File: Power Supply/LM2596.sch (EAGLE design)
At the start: 11 parts

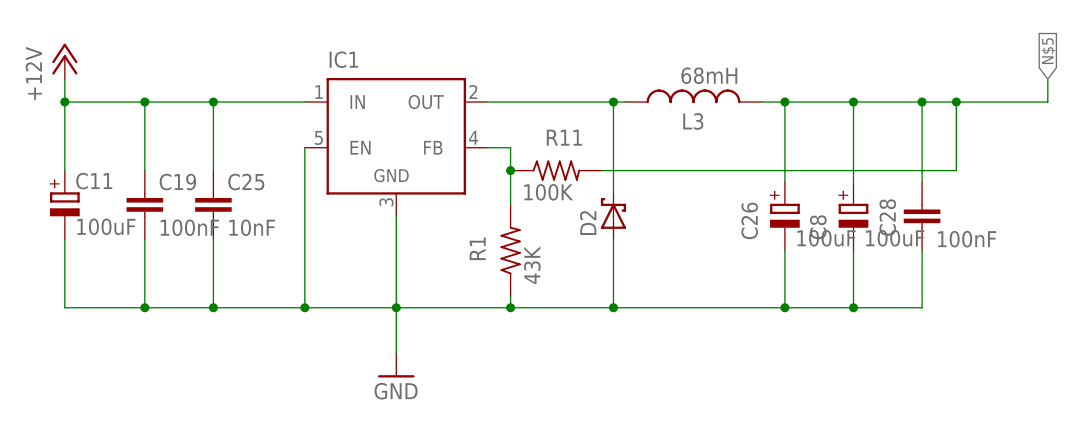
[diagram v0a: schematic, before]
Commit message: vcc updated in the circuit
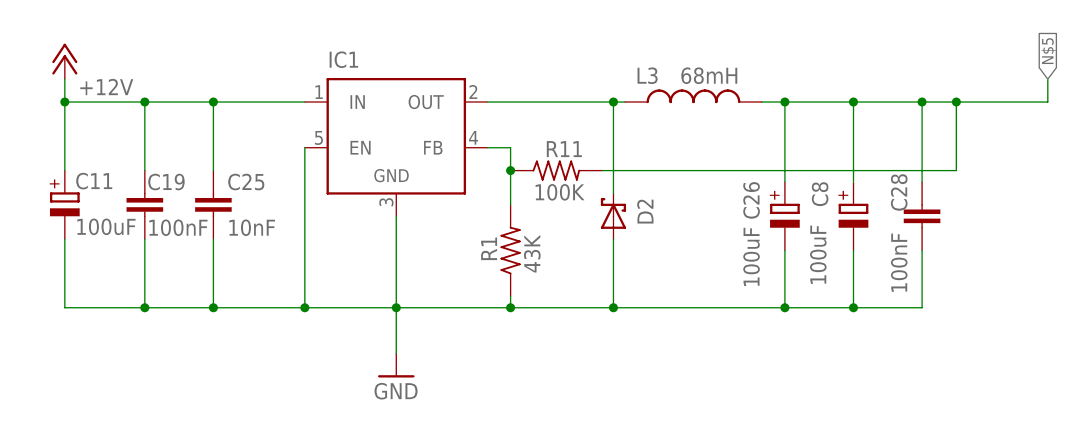
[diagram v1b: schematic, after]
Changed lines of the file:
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@@
 <layer number="94" name="Symbols" color="4" fill="1" visible="yes" active="yes"/>
 <layer number="95" name="Names" color="7" fill="1" visible="yes" active="yes"/>
-<layer number="96" name="Values" color="7" fill="1" visible="no" active="yes"/>
+<layer number="96" name="Values" color="7" fill="1" visible="yes" active="yes"/>
 <layer number="97" name="Info" color="7" fill="1" visible="yes" active="yes"/>
 <layer number="98" name="Guide" color="6" fill="1" visible="yes" active="yes"/>
@@
 </instance>
 <instance part="C26" gate="G$1" x="43.18" y="-8.89" smashed="yes">
-<attribute name="NAME" x="40.1574" y="-12.827" size="1.778" layer="95" rot="R90"/>
-<attribute name="VALUE" x="44.323" y="-13.4874" size="1.778" layer="96"/>
+<attribute name="NAME" x="38.5826" y="-6.223" size="1.778" layer="95" rot="R270"/>
+<attribute name="VALUE" x="38.5826" y="-11.303" size="1.778" layer="96" rot="R270"/>
 </instance>
 <instance part="C28" gate="G$1" x="58.42" y="-8.89" smashed="yes">
-<attribute name="NAME" x="55.499" y="-12.446" size="1.778" layer="95" rot="R90"/>
-<attribute name="VALUE" x="59.944" y="-13.589" size="1.778" layer="96"/>
+<attribute name="NAME" x="54.991" y="-5.334" size="1.778" layer="95" rot="R270"/>
+<attribute name="VALUE" x="56.769" y="-18.796" size="1.778" layer="96" rot="R90"/>
 </instance>
 <instance part="GND24" gate="1" x="0" y="-27.94" smashed="yes">
@@
 </instance>
 <instance part="P+1" gate="1" x="-36.83" y="7.62" smashed="yes">
-<attribute name="VALUE" x="-39.37" y="2.54" size="1.778" layer="96" rot="R90"/>
+<attribute name="VALUE" x="-29.21" y="5.08" size="1.778" layer="96" rot="R180"/>
 </instance>
 <instance part="D2" gate="G$1" x="24.13" y="-10.16" smashed="yes" rot="R90">
-<attribute name="NAME" x="22.225" y="-12.446" size="1.778" layer="95" rot="R90"/>
+<attribute name="NAME" x="28.575" y="-11.176" size="1.778" layer="95" rot="R90"/>
 <attribute name="VALUE" x="27.559" y="-12.446" size="1.778" layer="96" rot="R90"/>
 </instance>
@@
 </instance>
 <instance part="C8" gate="G$1" x="50.8" y="-8.89" smashed="yes">
-<attribute name="NAME" x="47.7774" y="-12.827" size="1.778" layer="95" rot="R90"/>
-<attribute name="VALUE" x="51.943" y="-13.4874" size="1.778" layer="96"/>
+<attribute name="NAME" x="46.2026" y="-6.223" size="1.778" layer="95" rot="R270"/>
+<attribute name="VALUE" x="47.7774" y="-17.907" size="1.778" layer="96" rot="R90"/>
 </instance>
 <instance part="C11" gate="G$1" x="-36.83" y="-7.62" smashed="yes">
@@
 </instance>
 <instance part="C19" gate="G$1" x="-27.94" y="-7.62" smashed="yes">
-<attribute name="NAME" x="-26.416" y="-7.239" size="1.778" layer="95"/>
-<attribute name="VALUE" x="-26.416" y="-12.319" size="1.778" layer="96"/>
+<attribute name="NAME" x="-27.686" y="-7.239" size="1.778" layer="95"/>
+<attribute name="VALUE" x="-27.686" y="-12.319" size="1.778" layer="96"/>
 </instance>
 <instance part="R11" gate="G$1" x="17.78" y="-5.08" smashed="yes">
-<attribute name="NAME" x="16.51" y="-2.3114" size="1.778" layer="95"/>
-<attribute name="VALUE" x="13.97" y="-8.382" size="1.778" layer="96"/>
+<attribute name="NAME" x="16.51" y="-3.5814" size="1.778" layer="95"/>
+<attribute name="VALUE" x="15.24" y="-8.382" size="1.778" layer="96"/>
 </instance>
 <instance part="R1" gate="G$1" x="12.7" y="-13.97" smashed="yes" rot="R90">
-<attribute name="NAME" x="9.9314" y="-15.24" size="1.778" layer="95" rot="R90"/>
-<attribute name="VALUE" x="16.002" y="-17.78" size="1.778" layer="96" rot="R90"/>
+<attribute name="NAME" x="11.2014" y="-15.24" size="1.778" layer="95" rot="R90"/>
+<attribute name="VALUE" x="16.002" y="-16.51" size="1.778" layer="96" rot="R90"/>
 </instance>
 <instance part="L3" gate="G$1" x="33.02" y="2.54" smashed="yes" rot="R90">
-<attribute name="NAME" x="34.29" y="1.27" size="1.778" layer="95" rot="R180"/>
+<attribute name="NAME" x="29.21" y="6.35" size="1.778" layer="95" rot="R180"/>
 <attribute name="VALUE" x="38.1" y="6.35" size="1.778" layer="96" rot="R180"/>
 </instance>
